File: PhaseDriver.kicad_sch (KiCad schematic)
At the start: 9 parts, among them Q1 EPC2088, Q8 EPC2088

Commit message: added license and almost ready for prod
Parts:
- C28, C29: Manufacturer_Part_Number (none) -> HHV1206R7475K101NSPJ; Rating (none) -> 100V
- C30: Rating (none) -> 100V
- D1, D2: Manufacturer_Part_Number (none) -> S3BB; Rating (none) -> 3A
- R33, R50: Rating (none) -> 4W
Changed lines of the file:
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@@
+			)
+		)
+		(property "Rating" "4W"
+			(at 102.87 85.09 0)
+			(effects
+				(font
+					(size 1.27 1.27)
+				)
+				(hide yes)
 			)
 		)
@@
 			)
 		)
+		(property "Rating" "4W"
+			(at 106.68 85.09 0)
+			(effects
+				(font
+					(size 1.27 1.27)
+				)
+				(hide yes)
+			)
+		)
 		(pin "2"
 		)
@@
 				)
 				(justify left)
+			)
+		)
+		(property "Rating" ""
+			(at 102.87 46.99 0)
+			(effects
+				(font
+					(size 1.27 1.27)
+				)
+				(hide yes)
 			)
 		)
@@
 			)
 		)
+		(property "Rating" "3A"
+			(at 132.08 64.77 0)
+			(effects
+				(font
+					(size 1.27 1.27)
+				)
+				(hide yes)
+			)
+		)
+		(property "Manufacturer_Part_Number" "S3BB"
+			(at 132.08 64.77 0)
+			(effects
+				(font
+					(size 1.27 1.27)
+				)
+				(hide yes)
+			)
+		)
 		(pin "2"
 		)
@@
 			)
 		)
+		(property "Rating" "3A"
+			(at 132.08 48.26 0)
+			(effects
+				(font
+					(size 1.27 1.27)
+				)
+				(hide yes)
+			)
+		)
+		(property "Manufacturer_Part_Number" "S3BB"
+			(at 132.08 48.26 0)
+			(effects
+				(font
+					(size 1.27 1.27)
+				)
+				(hide yes)
+			)
+		)
 		(pin "2"
 		)
@@
 			)
 		)
+		(property "Rating" "100V"
+			(at 78.74 58.42 0)
+			(effects
+				(font
+					(size 1.27 1.27)
+				)
+				(hide yes)
+			)
+		)
 		(pin "2"
 		)
@@
 			)
 		)
+		(property "Rating" ""
+			(at 102.87 68.58 0)
+			(effects
+				(font
+					(size 1.27 1.27)
+				)
+				(hide yes)
+			)
+		)
 		(pin "6"
 		)
@@
 			)
 		)
+		(property "Rating" "100V"
+			(at 52.07 58.42 0)
+			(effects
+				(font
+					(size 1.27 1.27)
+				)
+				(hide yes)
+			)
+		)
+		(property "Manufacturer_Part_Number" "HHV1206R7475K101NSPJ"
+			(at 52.07 58.42 0)
+			(effects
+				(font
+					(size 1.27 1.27)
+				)
+				(hide yes)
+			)
+		)
 		(pin "2"
 		)
@@
 			(at 64.77 58.42 0)
 			(effects
+				(font
+					(size 1.27 1.27)
+				)
+				(hide yes)
+			)
+		)
+		(property "Rating" "100V"
+			(at 64.77 58.42 0)
+			(effects
+				(font
+					(size 1.27 1.27)
+				)
+				(hide yes)
+			)
+		)
+		(property "Manufacturer_Part_Number" "HHV1206R7475K101NSPJ"
+			(at 64.77 58.42 0)
+			(effects

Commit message: first fab run
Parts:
- removed C29: 4.7uF, Capacitor_SMD:C_1206_3216Metric, symbol Device:C
- removed R33, R50: .5m, Resistor_SMD:R_1020_2550Metric, symbol Device:R_US
- added C14, C5: 100nF, Capacitor_SMD:C_0603_1608Metric, symbol Device:C
- added C20, C70, C73: 1uF, Capacitor_SMD:C_0805_2012Metric, symbol Device:C
- added C32: 4.7uF, Capacitor_SMD:C_1210_3225Metric, symbol Device:C
- C28: footprint Capacitor_SMD:C_1206_3216Metric -> Capacitor_SMD:C_1210_3225Metric; Manufacturer_Part_Number HHV1206R7475K101NSPJ -> FS32X475K101EGG; Source (none) -> LCSC
- C30: Manufacturer_Part_Number (none) -> CGA0603X7R104K101JT; Source (none) -> LCSC
- D1, D2: value S3BB-13-F -> .85V; Manufacturer_Part_Number S3BB -> SS310; Source (none) -> LCSC
- Q1, Q8: value EPC2088 -> EPC2065; Manufacturer_Part_Number (none) -> EPC2065; Rating (none) -> 80V 60A; Source (none) -> Digikey
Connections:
- net I_SENSE is gone; now on net GND: Q1.2 (S), Q1.4 (S), Q1.6 (S), Q1.8 (S)
- net GND: now also C14.2, C20.2, C32.2, C5.2, C70.2, C73.2
- net V_{DRV}: now also C14.1, C20.1, C32.1, C5.1, C70.1, C73.1
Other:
- moved on the sheet: C30, D1, D2, Q1, Q8

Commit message: Production round 1
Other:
- note added: "0-80V 0-60A"
- note added: "Flyback Diodes"
- note added: "High Frequency Caps"
- note added: "Low Frequency Caps"
- note added: "Medium Frequency Caps"
- note removed: "0-100V 0-60A"
- note removed: "Flyback Diode"
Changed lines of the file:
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@@
 	(wire
 		(pts
-			(xy 176.53 55.88) (xy 182.88 55.88)
+			(xy 176.53 55.88) (xy 186.69 55.88)
 		)
 		(stroke
@@
 	(rectangle
 		(start 171.45 34.29)
-		(end 181.61 54.61)
+		(end 185.42 76.2)
 		(stroke
 			(width 0)
@@
 		)
 	)
-	(text "0-100V 0-60A"
+	(rectangle
+		(start 58.42 36.83)
+		(end 97.155 85.09)
+		(stroke
+			(width 0)
+			(type dash_dot)
+		)
+		(fill
+			(type none)
+		)
+	)
+	(rectangle
+		(start 97.155 36.83)
+		(end 133.35 85.09)
+		(stroke
+			(width 0)
+			(type dot)
+		)
+		(fill
+			(type none)
+		)
+	)
+	(rectangle
+		(start 31.75 36.83)
+		(end 58.42 85.09)
+		(stroke
+			(width 0)
+			(type dash)
+		)
+		(fill
+			(type none)
+		)
+	)
+	(text "0-80V 0-60A"
 		(exclude_from_sim no)
 		(at 74.422 32.258 0)
@@
 		)
 	)
-	(text "Flyback Diode"
+	(text "Medium Frequency Caps"
+		(exclude_from_sim no)
+		(at 76.454 35.56 0)
+		(effects
+			(font
+				(size 1.27 1.27)
+			)
+		)
+	)
+	(text "High Frequency Caps"
+		(exclude_from_sim no)
+		(at 113.03 35.56 0)
+		(effects
+			(font
+				(size 1.27 1.27)
+			)
+		)
+	)
+	(text "Low Frequency Caps"
+		(exclude_from_sim no)
+		(at 45.72 35.814 0)
+		(effects
+			(font
+				(size 1.27 1.27)
+			)
+		)
+	)
+	(text "Flyback Diodes"
 		(exclude_from_sim no)
 		(at 171.196 32.258 0)
@@
 	(hierarchical_label "PHASE"
 		(shape bidirectional)
-		(at 182.88 55.88 0)
+		(at 186.69 55.88 0)
 		(fields_autoplaced yes)
 		(effects
@@
 			)
 		)
-		(property "Description" "100 V 60A 3.2mE"
+		(property "Description" "80 V 60A 3.2mE"
 			(at 151.13 48.006 0)
 			(effects
@@
 			)
 		)
-		(property "Description" "100 V 60A 3.2mE"
+		(property "Description" "80 V 60A 3.2mE"
 			(at 151.13 69.8499 0)
 			(effects

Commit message: more powerful version
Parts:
- removed Q1, Q8: EPC2065, EPC_FETs:D0320T34M, symbol EPC_FETs:EPC2088
- added Q1, Q4: EPC2302, EPC_FETs:D0606F_100V, symbol EPC_FETs:EPC2302
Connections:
- net GND: now also Q1.2 (S), Q1.4 (S), Q1.6 (S)
- net HIGH: now also Q4.1 (G)
- net LOW: now also Q1.1 (G)
- net PHASE: now also Q1.3 (D), Q1.5 (D), Q1.7 (D), Q4.2 (S), Q4.4 (S), Q4.6 (S)
- net V_{DRV}: now also Q4.3 (D), Q4.5 (D), Q4.7 (D)

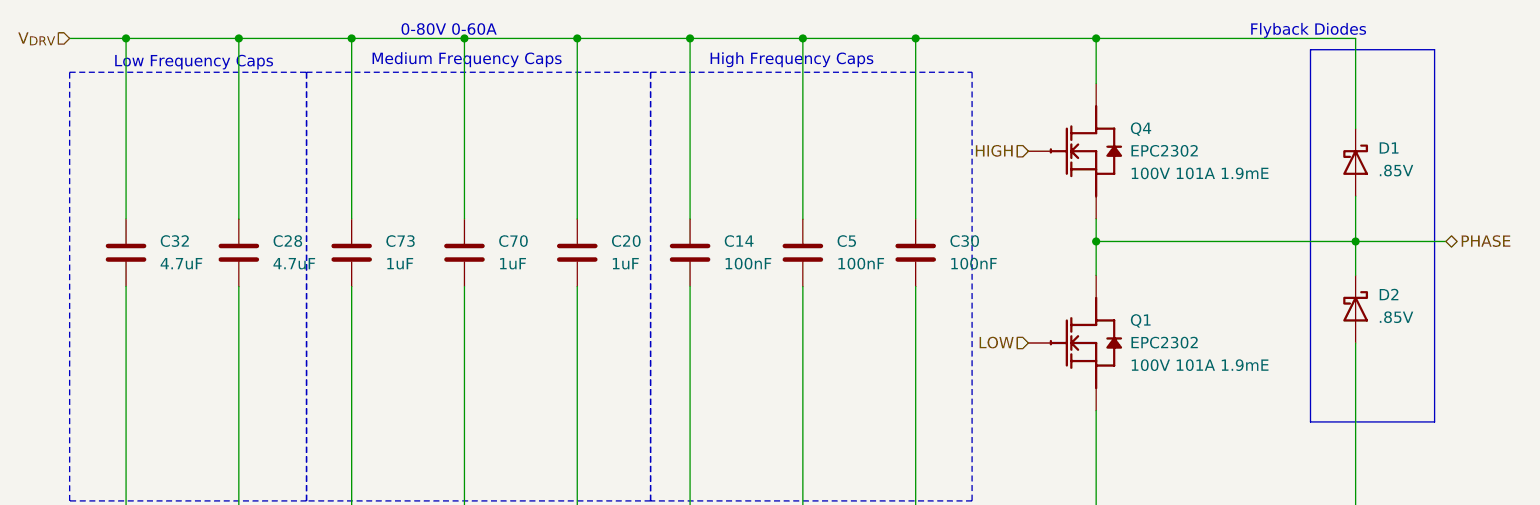
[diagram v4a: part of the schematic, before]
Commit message: adjusted according to Reddit feedback
Still needs TVS adjusted
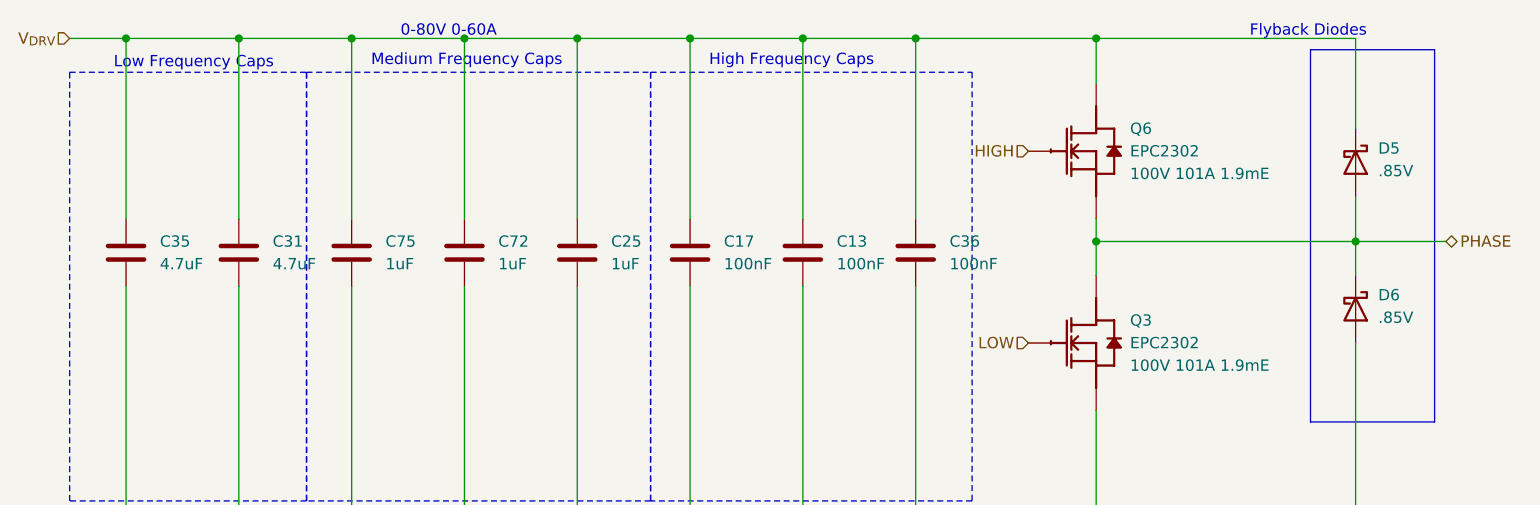
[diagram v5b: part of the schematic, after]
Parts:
- renumbered C5 to C13, C14 to C17, C20 to C25, C28 to C31, C32 to C35, C30 to C36, C70 to C72, C73 to C75, D1 to D5, D2 to D6, Q1 to Q3, Q4 to Q6
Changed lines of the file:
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@@
 		(dnp no)
 		(fields_autoplaced yes)
-		(property "Reference" "C5"
+		(property "Reference" "C13"
 			(at 118.11 55.8799 0)
 			(effects
@@
 		(dnp no)
 		(fields_autoplaced yes)
-		(property "Reference" "Q4"
+		(property "Reference" "Q6"
 			(at 151.13 43.1799 0)
 			(effects
@@
 		(dnp no)
 		(fields_autoplaced yes)
-		(property "Reference" "D2"
+		(property "Reference" "D6"
 			(at 179.07 61.9124 90)
 			(effects
@@
 		(dnp no)
 		(fields_autoplaced yes)
-		(property "Reference" "D1"
+		(property "Reference" "D5"
 			(at 179.07 45.4024 90)
 			(effects
@@
 		(dnp no)
 		(fields_autoplaced yes)
-		(property "Reference" "C30"
+		(property "Reference" "C36"
 			(at 130.81 55.8799 0)
 			(effects
@@
 		(dnp no)
 		(fields_autoplaced yes)
-		(property "Reference" "C14"
+		(property "Reference" "C17"
 			(at 105.41 55.8799 0)
 			(effects
@@
 		(dnp no)
 		(fields_autoplaced yes)
-		(property "Reference" "C32"
+		(property "Reference" "C35"
 			(at 41.91 55.8799 0)
 			(effects
@@
 		(dnp no)
 		(fields_autoplaced yes)
-		(property "Reference" "Q1"
+		(property "Reference" "Q3"
 			(at 151.13 64.7699 0)
 			(effects
@@
 		(dnp no)
 		(fields_autoplaced yes)
-		(property "Reference" "C73"
+		(property "Reference" "C75"
 			(at 67.31 55.8799 0)
 			(effects
@@
 		(dnp no)
 		(fields_autoplaced yes)
-		(property "Reference" "C28"
+		(property "Reference" "C31"
 			(at 54.61 55.8799 0)
 			(effects
@@
 		(dnp no)
 		(fields_autoplaced yes)
-		(property "Reference" "C20"
+		(property "Reference" "C25"
 			(at 92.71 55.8799 0)
 			(effects
@@
 		(dnp no)
 		(fields_autoplaced yes)
-		(property "Reference" "C70"
+		(property "Reference" "C72"
 			(at 80.01 55.8799 0)
 			(effects

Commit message: added all changes from Reddit
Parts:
- added C56, C83: C, Capacitor_SMD:C_0603_1608Metric, symbol Device:C
- added D27, D30: 6V, Diode_SMD:D_SOD-323, symbol Device:D_Zener_Small_Filled
- added R38, R41: R, Resistor_SMD:R_0603_1608Metric, symbol Device:R_US
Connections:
- net GND: now also C83.2, D30.2 (A)
- net HIGH: now also D27.1 (K)
- net LOW: now also D30.1 (K)
- net PHASE: now also C56.2, D27.2 (A), R41.1
- net V_{DRV}: now also R38.1
- new net: C56.1, R38.2
- new net: C83.1, R41.2
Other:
- moved on the sheet: C13, C17, C25, C31, C35, C36, C72, C75, D5, D6, Q3, Q6

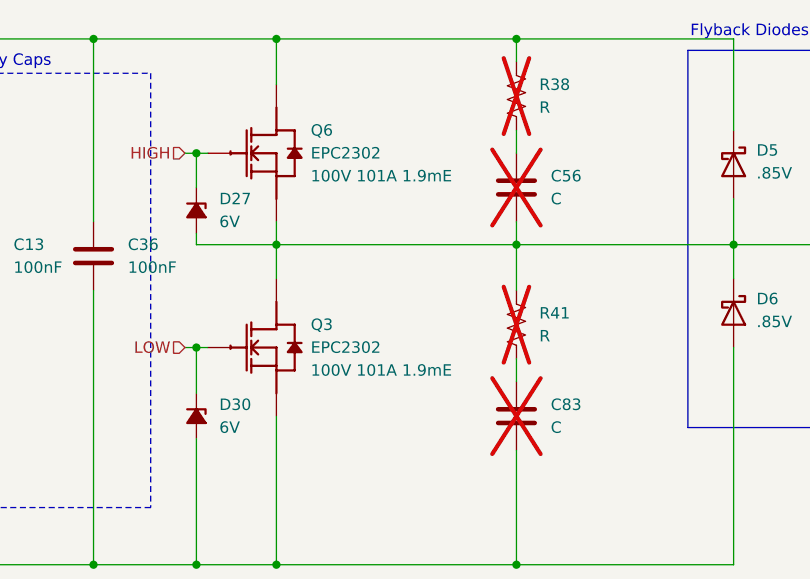
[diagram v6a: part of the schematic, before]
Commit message: Removed Hall Sensors for Scalability
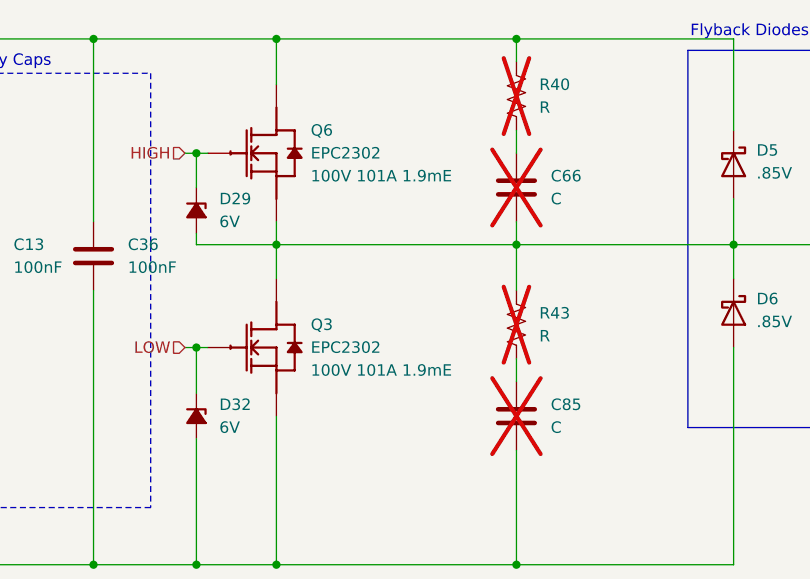
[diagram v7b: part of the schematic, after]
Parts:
- renumbered C56 to C66, C83 to C85, D27 to D29, D30 to D32, R38 to R40, R41 to R43
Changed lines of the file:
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@@
 		(dnp yes)
 		(fields_autoplaced yes)
-		(property "Reference" "R38"
+		(property "Reference" "R40"
 			(at 195.58 73.6599 0)
 			(effects
@@
 		(dnp no)
 		(fields_autoplaced yes)
-		(property "Reference" "D27"
+		(property "Reference" "D29"
 			(at 160.02 86.3599 90)
 			(effects
@@
 		(dnp no)
 		(fields_autoplaced yes)
-		(property "Reference" "D30"
+		(property "Reference" "D32"
 			(at 160.02 109.2199 90)
 			(effects
@@
 		(dnp yes)
 		(fields_autoplaced yes)
-		(property "Reference" "C56"
+		(property "Reference" "C66"
 			(at 196.85 83.8199 0)
 			(effects
@@
 		(dnp yes)
 		(fields_autoplaced yes)
-		(property "Reference" "R41"
+		(property "Reference" "R43"
 			(at 195.58 99.0599 0)
 			(effects
@@
 		(dnp yes)
 		(fields_autoplaced yes)
-		(property "Reference" "C83"
+		(property "Reference" "C85"
 			(at 196.85 109.2199 0)
 			(effects

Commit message: updates to make better
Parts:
- C31, C35: value 4.7uF -> 10uF
- C66, C85, R40, R43: Manufacturer_Part_Number (none) -> N/A; Source (none) -> N/A
- D29, D32: Manufacturer_Part_Number (none) -> MMSZ5233BS-7-F; Source (none) -> LCSC
- Q3, Q6: Manufacturer_Part_Number (none) -> EPC2302; Source (none) -> Digikey
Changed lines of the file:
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@@
+			)
+		)
+		(property "Manufacturer_Part_Number" "EPC2302"
+			(at 166.37 81.28 0)
+			(effects
+				(font
+					(size 1.27 1.27)
+				)
+				(hide yes)
+			)
+		)
+		(property "Source" "Digikey"
+			(at 166.37 81.28 0)
+			(effects
+				(font
+					(size 1.27 1.27)
+				)
+				(hide yes)
 			)
 		)
@@
 			)
 		)
+		(property "Manufacturer_Part_Number" "N/A"
+			(at 193.04 74.93 0)
+			(effects
+				(font
+					(size 1.27 1.27)
+				)
+				(hide yes)
+			)
+		)
+		(property "Source" "N/A"
+			(at 193.04 74.93 0)
+			(effects
+				(font
+					(size 1.27 1.27)
+				)
+				(hide yes)
+			)
+		)
 		(pin "2"
 		)
@@
 			)
 		)
+		(property "Manufacturer_Part_Number" "MMSZ5233BS-7-F"
+			(at 157.48 87.63 0)
+			(effects
+				(font
+					(size 1.27 1.27)
+				)
+				(hide yes)
+			)
+		)
+		(property "Source" "LCSC"
+			(at 157.48 87.63 0)
+			(effects
+				(font
+					(size 1.27 1.27)
+				)
+				(hide yes)
+			)
+		)
 		(pin "2"
 		)
@@
 			)
 		)
+		(property "Manufacturer_Part_Number" "MMSZ5233BS-7-F"
+			(at 157.48 110.49 0)
+			(effects
+				(font
+					(size 1.27 1.27)
+				)
+				(hide yes)
+			)
+		)
+		(property "Source" "LCSC"
+			(at 157.48 110.49 0)
+			(effects
+				(font
+					(size 1.27 1.27)
+				)
+				(hide yes)
+			)
+		)
 		(pin "2"
 		)
@@
 			)
 		)
-		(property "Value" "4.7uF"
+		(property "Value" "10uF"
 			(at 60.96 93.9799 0)
 			(effects
@@
 			)
 		)
+		(property "Manufacturer_Part_Number" "EPC2302"
+			(at 166.37 102.87 0)
+			(effects
+				(font
+					(size 1.27 1.27)
+				)
+				(hide yes)
+			)
+		)
+		(property "Source" "Digikey"
+			(at 166.37 102.87 0)
+			(effects
+				(font
+					(size 1.27 1.27)
+				)
+				(hide yes)
+			)
+		)
 		(pin "3"
 		)
@@
 			)
 		)
-		(property "Value" "4.7uF"
+		(property "Value" "10uF"
 			(at 73.66 93.9799 0)
 			(effects
@@
 			)
 		)
+		(property "Manufacturer_Part_Number" "N/A"
+			(at 193.04 85.09 0)
+			(effects
+				(font
+					(size 1.27 1.27)
+				)
+				(hide yes)
+			)
+		)
+		(property "Source" "N/A"
+			(at 193.04 85.09 0)
+			(effects
+				(font
+					(size 1.27 1.27)
+				)
+				(hide yes)
+			)
+		)
 		(pin "2"
 		)
@@
 			)
 		)
+		(property "Manufacturer_Part_Number" "N/A"
+			(at 193.04 100.33 0)
+			(effects
+				(font
+					(size 1.27 1.27)
+				)
+				(hide yes)
+			)
+		)
+		(property "Source" "N/A"
+			(at 193.04 100.33 0)
+			(effects
+				(font
+					(size 1.27 1.27)
+				)
+				(hide yes)
+			)
+		)
 		(pin "2"
 		)
@@
 			(at 193.04 110.49 0)
 			(effects
+				(font
+					(size 1.27 1.27)
+				)
+				(hide yes)
+			)
+		)
+		(property "Manufacturer_Part_Number" "N/A"
+			(at 193.04 110.49 0)
+			(effects
+				(font
+					(size 1.27 1.27)
+				)
+				(hide yes)
+			)
+		)
+		(property "Source" "N/A"
+			(at 193.04 110.49 0)
+			(effects
